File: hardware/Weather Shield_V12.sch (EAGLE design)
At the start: 51 parts, among them J1 GP-635T, Q1 BSS138, Q2 BSS138, U1 ARDUINO_R3_SHIELD, U2 3.3V MIC5219, U3 ALS-PT19, U4 MPL3115A2LGA8

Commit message: Post group review changes
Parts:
- added JP1: JUMPER-PAD-2-NC_BY_TRACENO_SILK, SparkFun-Passives:JUMPER-PAD-2-NC_BY_TRACENO_SILK
- renumbered U$1 to U5
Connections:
- net RAW renamed VIN
- new net N$6: JP1.1, U1.D12
- net INT-PRESSURE: now also JP1.2
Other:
- note added: "LEDs"
- moved on the sheet: D1, D3, R1, R10, R6, R7, R8, U1, U3

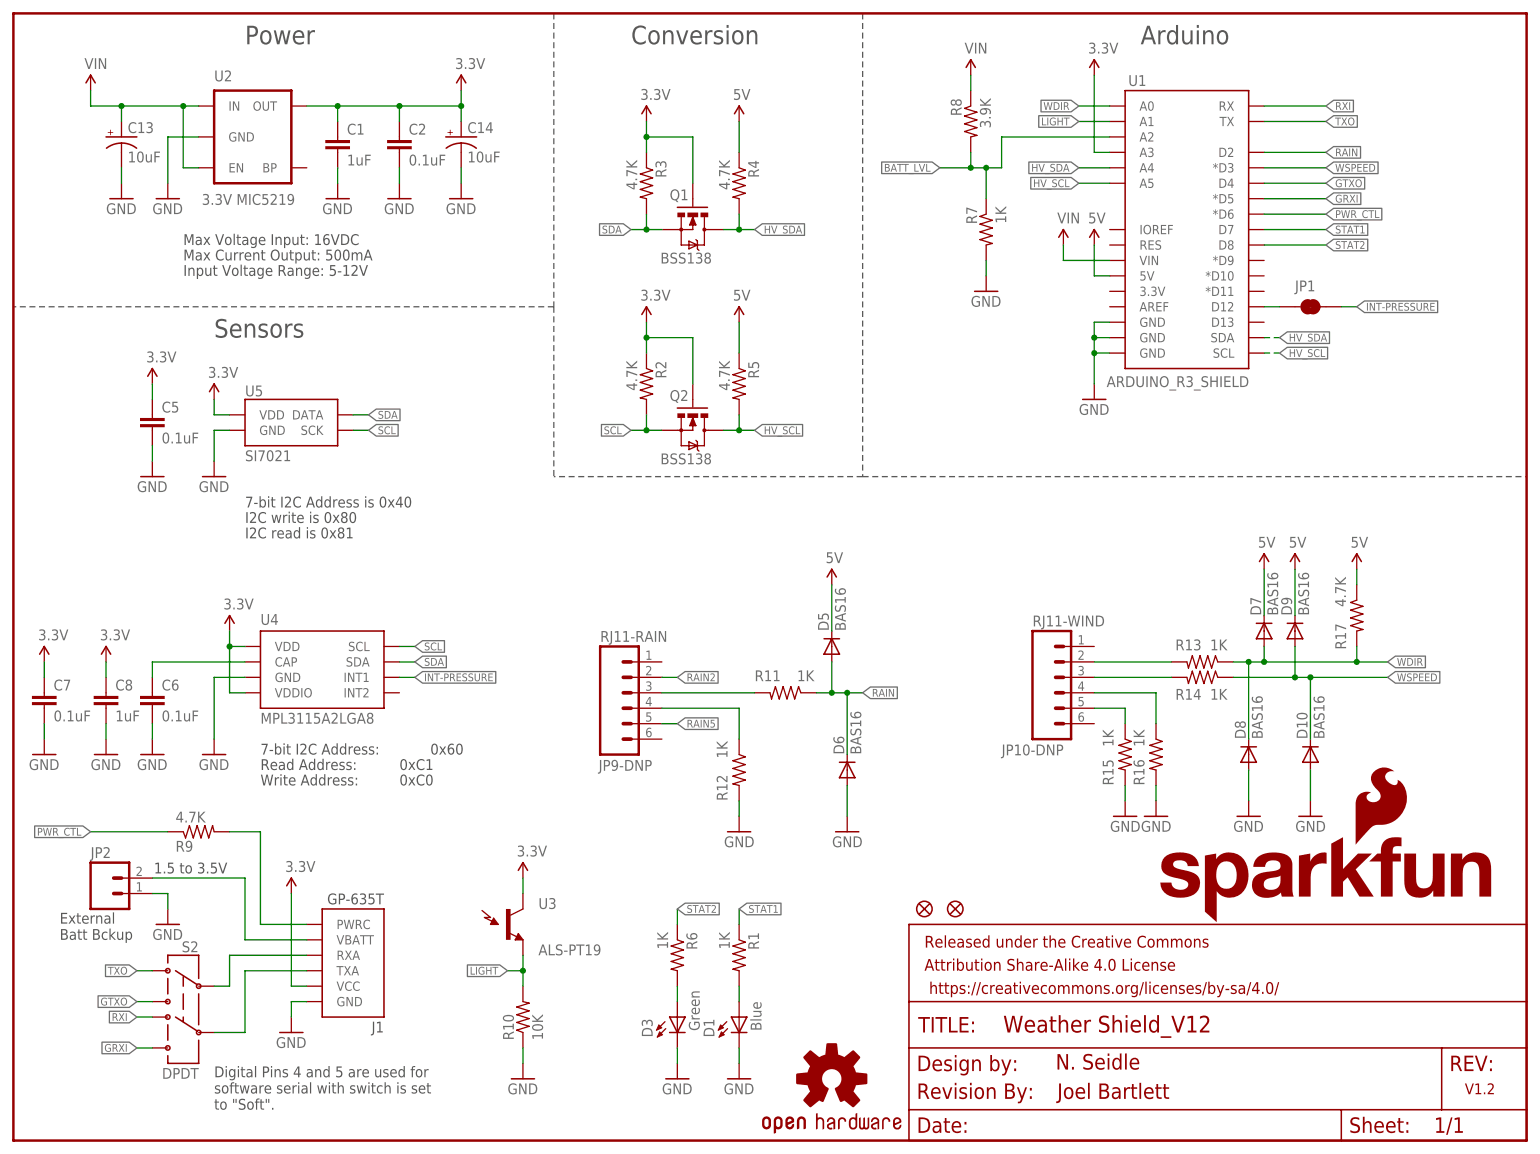
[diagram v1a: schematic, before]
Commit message: Post QC Checklist fixes
Addressed the few issues that came up during the preliminary QC
checklist. Mostly PROD_IDs missing and aesthetic fixes.
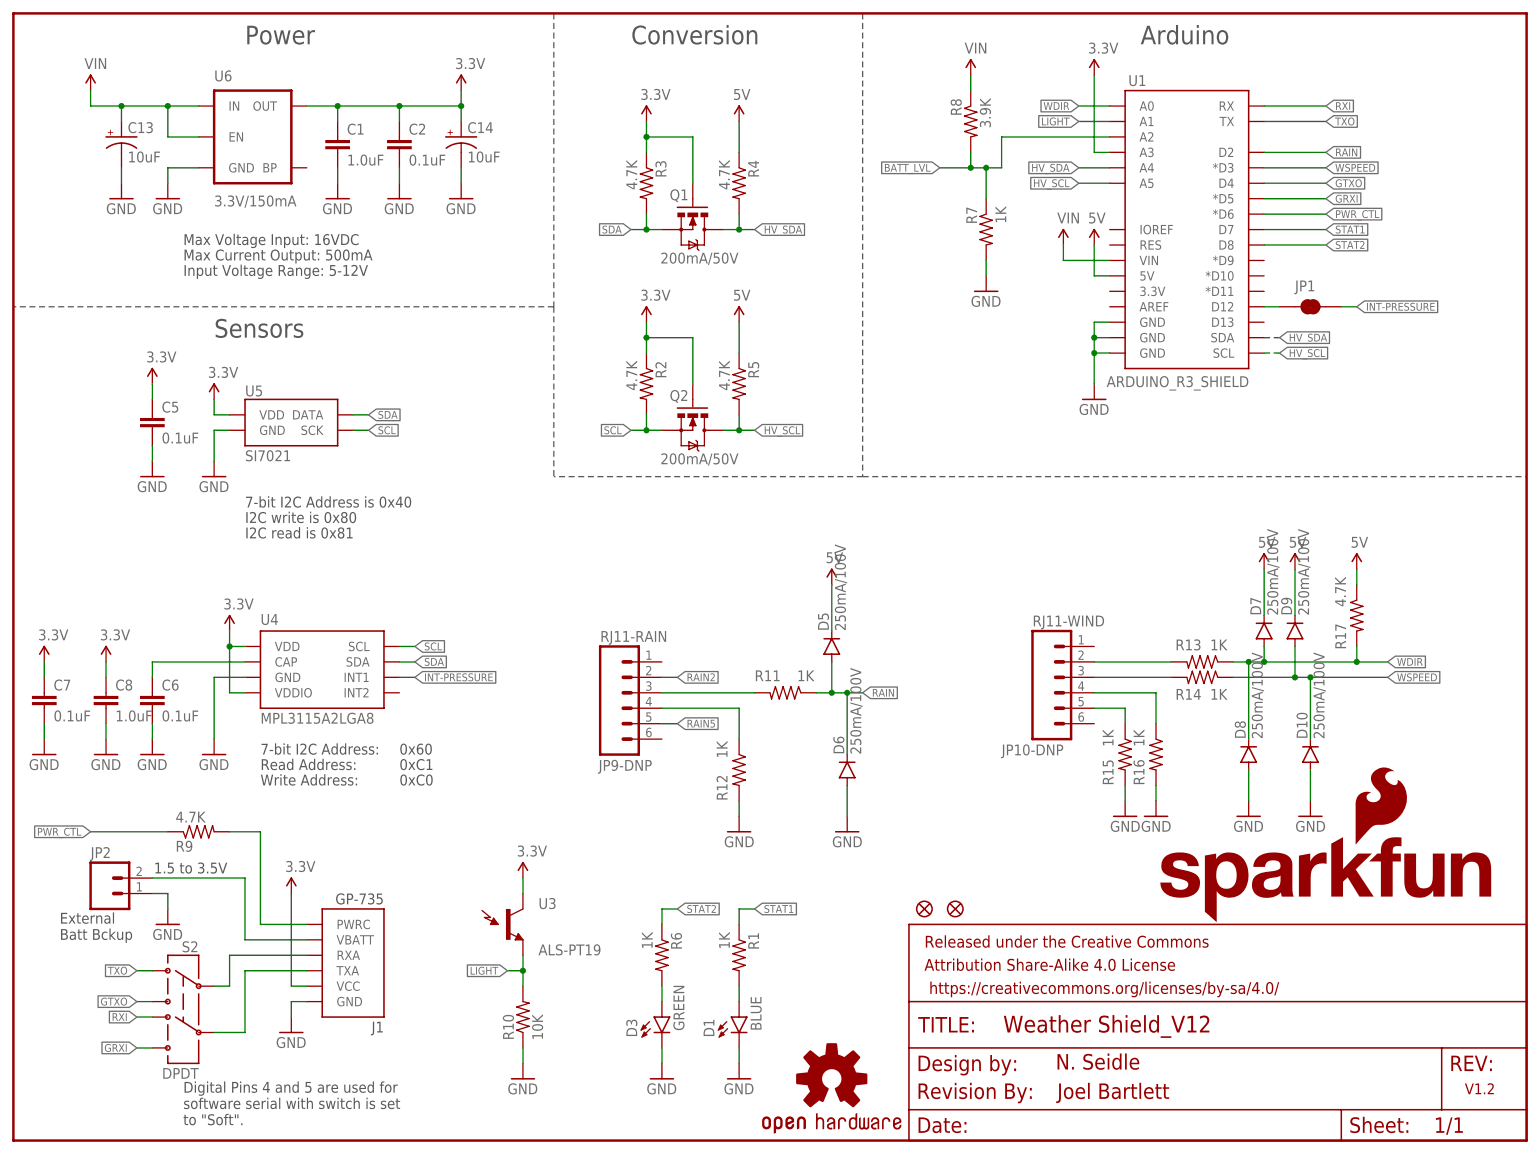
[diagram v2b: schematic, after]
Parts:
- removed U2: 3.3V MIC5219, SparkFun:V_REG_LDOSMD
- added U6: 3.3V/150mA, SparkFun-PowerIC:V_REG_MIC52053.3V
- C1, C8: value 1uF -> 1.0uF; device SparkFun:CAP0603-CAP -> SparkFun-Capacitors:1.0UF-16V-10%(0603)
- C13, C14: device SparkFun-Passives:CAP_POL1206 -> SparkFun-Capacitors:10UF-16V-10%(TANT)
- C2, C5, C6, C7: device SparkFun:CAP0603-CAP -> SparkFun-Capacitors:0.1UF-25V(+80/-20%)(0603)
- D1: value Blue -> BLUE; device SparkFun:LED0603 -> SparkFun-LED:LED-BLUE0603
- D10, D5, D6, D7, D8, D9: value BAS16 -> 250mA/100V; device SparkFun:DIODESOD -> SparkFun-DiscreteSemi:DIODEBAS16
- D3: value Green -> GREEN; device SparkFun:LED0603 -> SparkFun-LED:LED-GREEN0603
- J1: value GP-635T -> GP-735
- JP10-DNP, JP9-DNP: device SparkFun:RJ11-6PTH -> SparkFun-Connectors:RJ11-6PTH
- Q1, Q2: value BSS138 -> 200mA/50V; device SparkFun:MOSFET-NCHANNELSMD -> SparkFun-DiscreteSemi:MOSFET-NCHANNELBSS138
- R1, R11, R12, R13, R14, R15, R16, R6, R7: device SparkFun:RESISTOR0603-RES -> SparkFun-Resistors:1KOHM-1/10W-1%(0603)
- R10: device SparkFun-Passives:RESISTOR0603-RES -> SparkFun-Resistors:10KOHM-1/10W-1%(0603)0603
- R17, R2, R3, R4, R5, R9: device SparkFun:RESISTOR0603-RES -> SparkFun-Resistors:4.7KOHM-1/10W-1%(0603)
- R8: device SparkFun:RESISTOR0603-RES -> SparkFun-Resistors:3.9KOHM1/10W1%(0603)
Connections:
- net 3.3V: now also U6.OUT; no longer U2.OUT
- net GND: now also U6.GND; no longer U2.GND
- net VIN: now also U6.EN, U6.IN; no longer U2.EN, U2.IN
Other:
- moved on the sheet: R6
